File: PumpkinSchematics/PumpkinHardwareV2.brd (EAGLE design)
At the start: 80.8 x 84.8 mm, 21 parts, among them IC1 ATMEGA48/88/168-PU, X2 22-23-2041

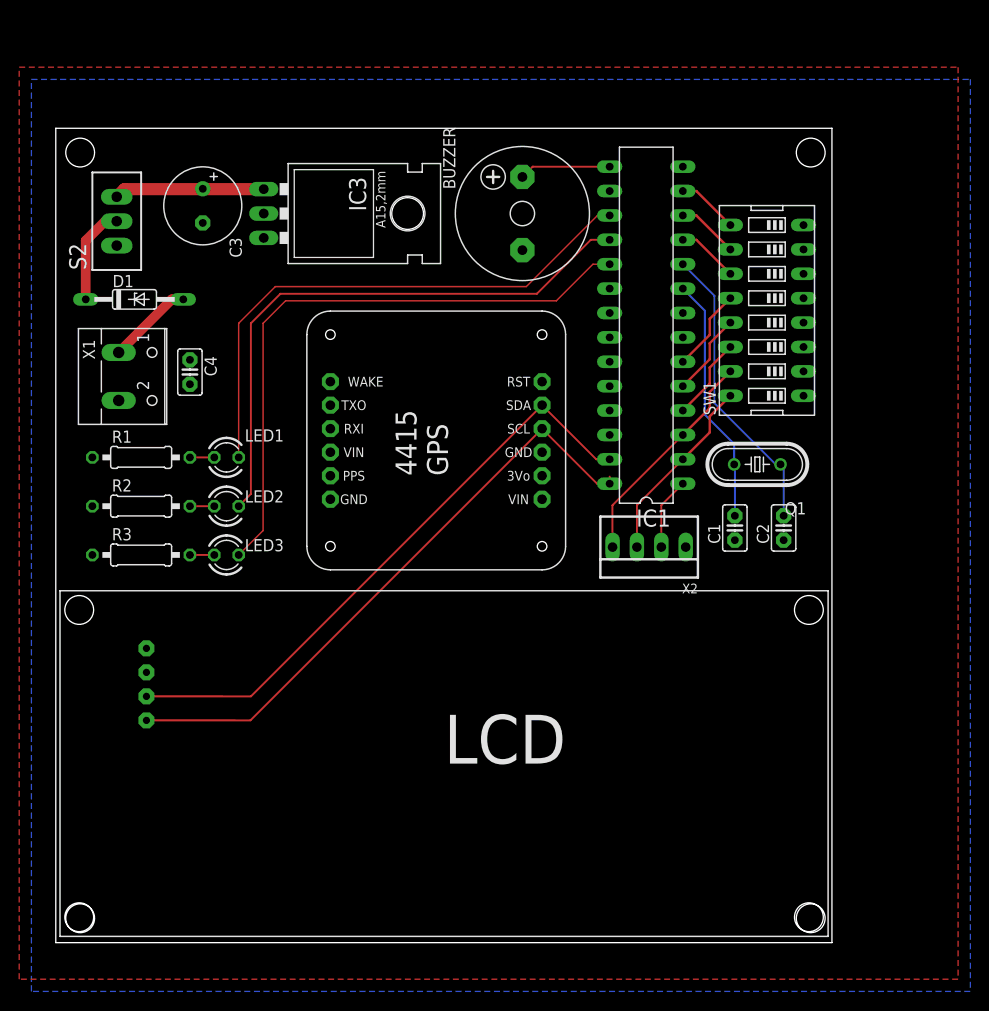
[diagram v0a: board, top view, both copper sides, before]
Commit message: added interrupt for simulation updates
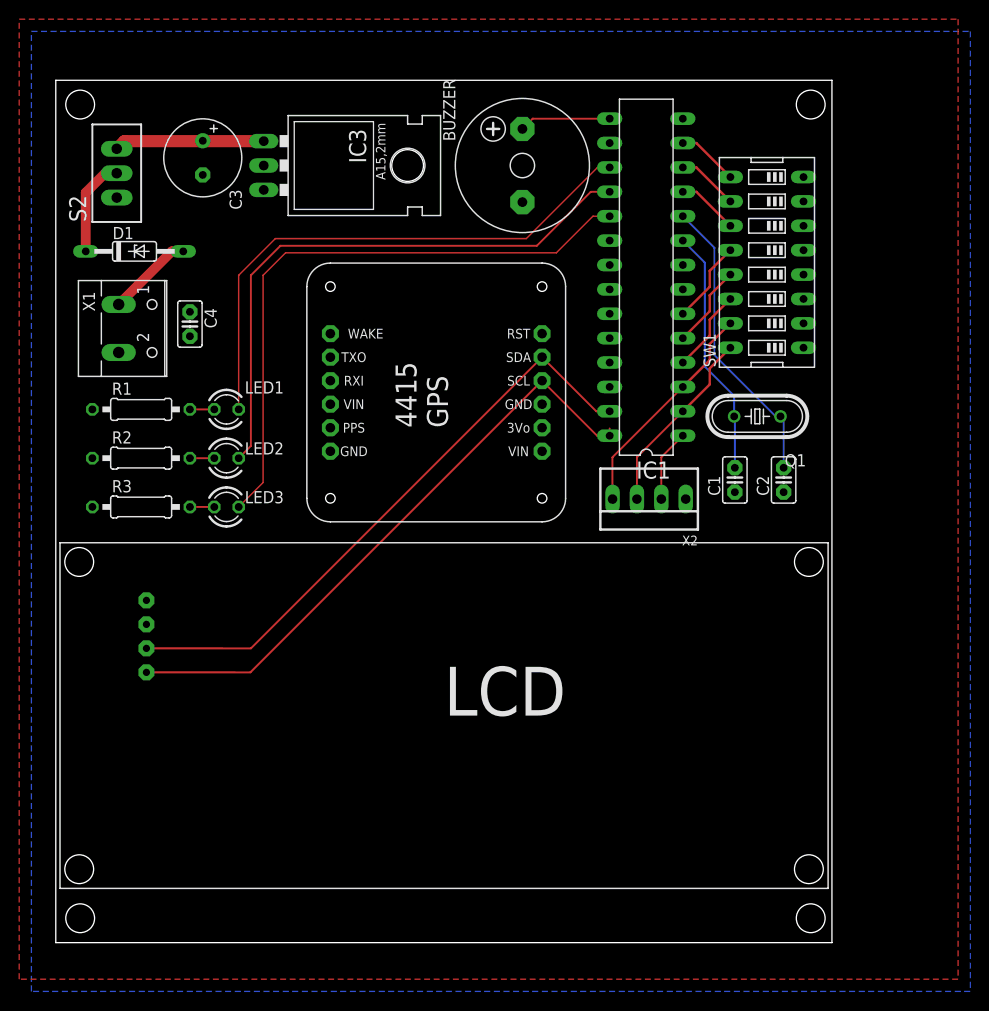
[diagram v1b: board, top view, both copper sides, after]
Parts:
- moved C4 5.00 mm to (14.0, 64.4)
- moved BUZZER 5.00 mm to (48.6, 80.9)
- moved C1 5.00 mm to (70.7, 48.2)
- moved C2 5.00 mm to (75.8, 48.2)
- moved C3 5.00 mm to (15.3, 81.7)
- moved D1 5.00 mm to (8.20, 72.0)
- moved GPS 5.00 mm to (40.4, 56.5)
- moved IC1 5.00 mm to (61.5, 69.3)
- moved IC3 5.00 mm to (25.5, 80.9)
- moved LED1 5.00 mm to (17.8, 55.5)
- moved LED2 5.00 mm to (17.8, 50.5)
- moved LED3 5.00 mm to (17.8, 45.4)
- moved Q1 5.00 mm to (73.1, 54.8)
- moved R1 5.00 mm to (8.89, 55.5)
- moved R2 5.00 mm to (8.89, 50.5)
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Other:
- board size 80.8 x 84.8 mm -> 80.8 x 89.8 mm
